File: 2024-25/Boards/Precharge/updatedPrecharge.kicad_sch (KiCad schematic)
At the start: 22 parts, among them J2 43045-0812, Q1 DMN2056U, Q2 DMP2035U, Q3 DMP2035U, Q4 DMP2035U, U1 LM358DR2G

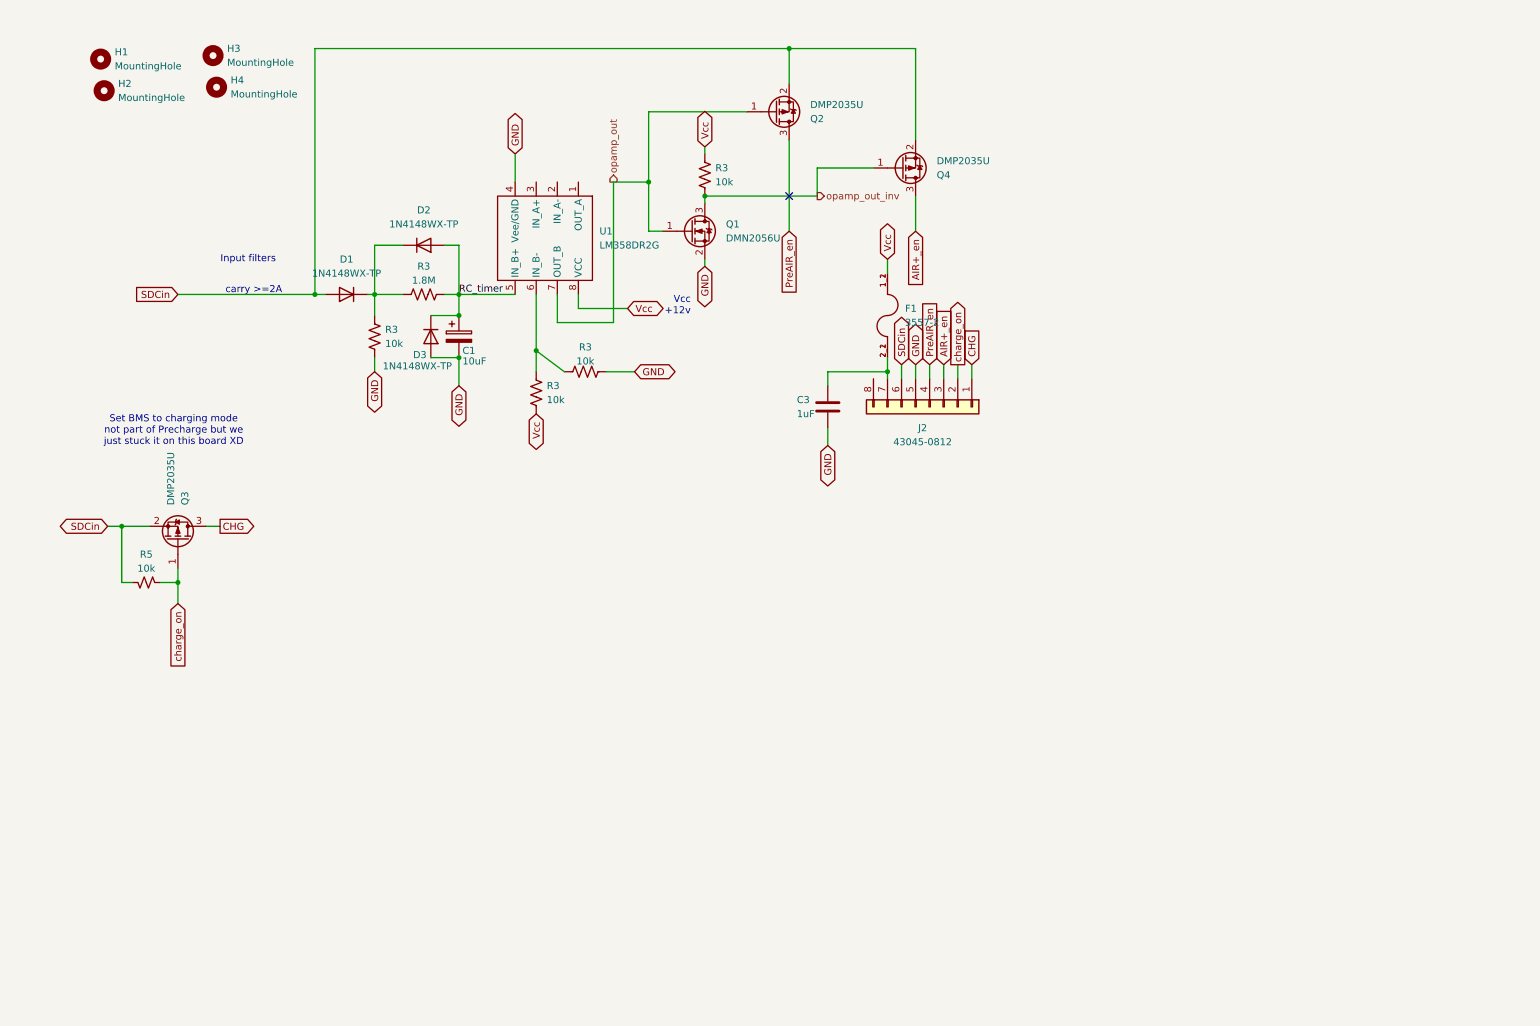
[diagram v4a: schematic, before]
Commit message: new Precharge circuit schm
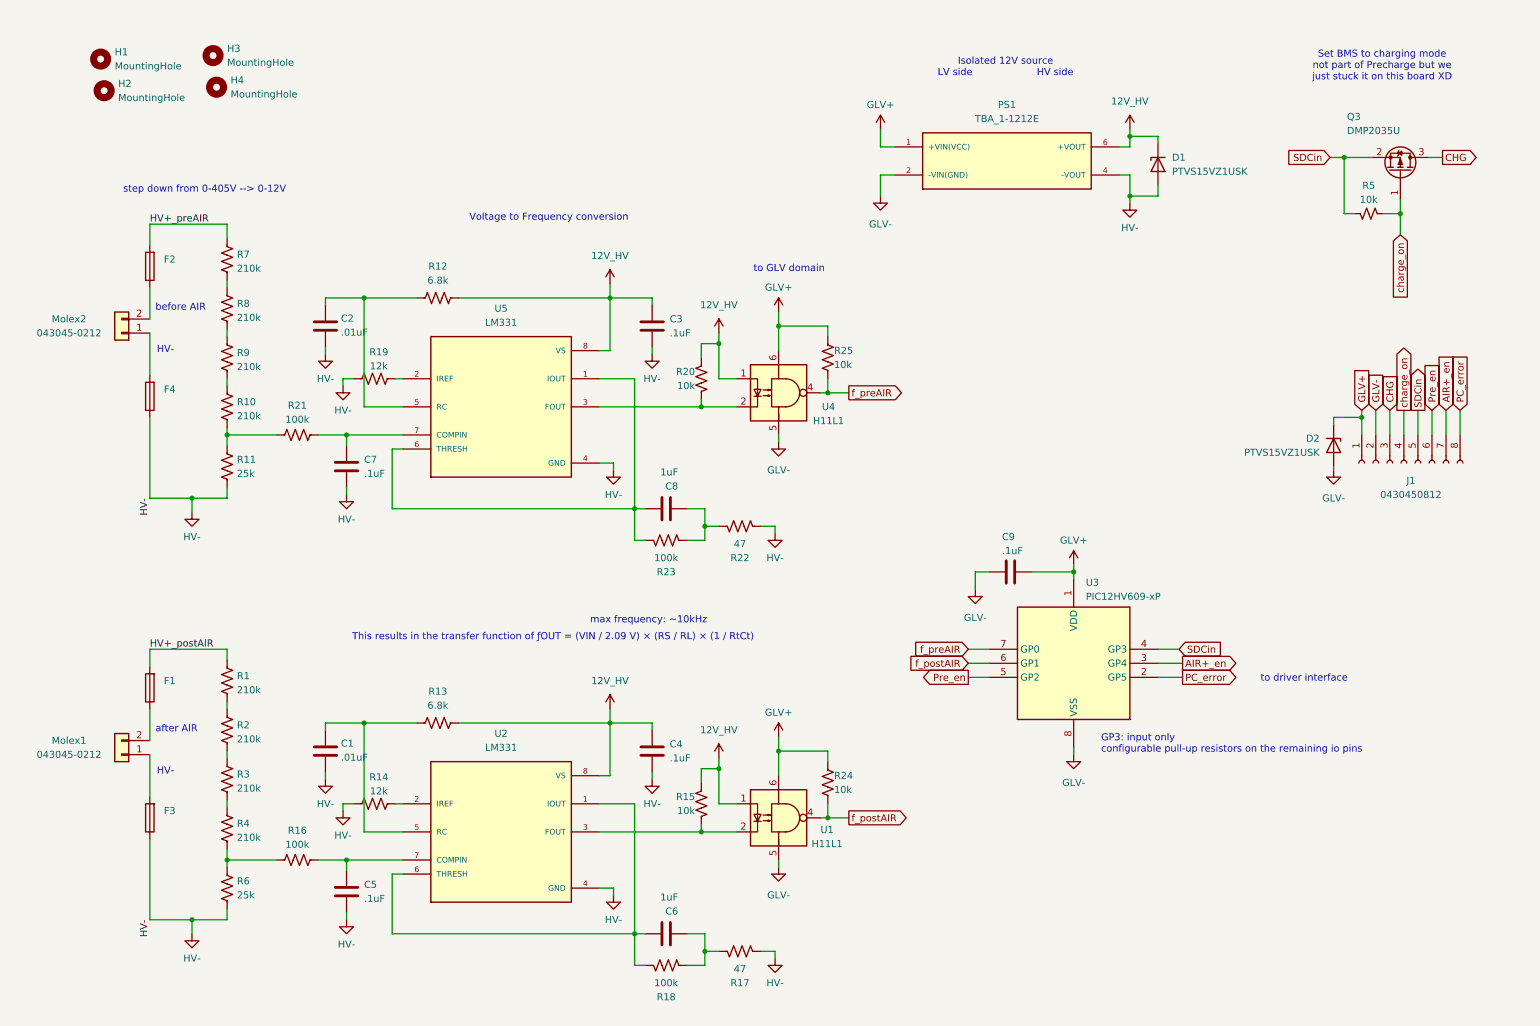
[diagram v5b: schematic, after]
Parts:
- removed C1: 10uF, Capacitor_SMD:C_1206_3216Metric_Pad1.33x1.80mm_HandSolder, symbol Device:C_Polarized
- removed D1, D2, D3: 1N4148WX-TP, Diode_SMD:D_SOD-323, symbol Diode:BAV302
- removed F1: 3557-2, Fuseholder:fuse, symbol 3557-2:3557-2
- removed J2: 43045-0812, Connector_Molex:Molex_Micro-Fit_3.0_43045-0812_2x04_P3.00mm_Vertical, symbol Connector_Generic:Conn_01x08
- removed Q1: DMN2056U, Package_TO_SOT_SMD:SOT-23, symbol Transistor_FET:DMN2056U
- removed Q2, Q4: DMP2035U, Package_TO_SOT_SMD:SOT-23, symbol Transistor_FET:AO3401A
- removed R3 (x4): 10k, Resistor_SMD:R_0805_2012Metric_Pad1.20x1.40mm_HandSolder, symbol Device:R_US
- removed R3: 1.8M, Resistor_SMD:R_0805_2012Metric_Pad1.20x1.40mm_HandSolder, symbol Device:R_US
- removed U1: LM358DR2G, Package_SO:SOIC-8_3.9x4.9mm_P1.27mm, symbol Amplifier_Operational:LM358_whole_unit
- added C1, C2: .01uF, Capacitor_SMD:C_0603_1608Metric, symbol Device:C
- added C4, C5, C7, C9: .1uF, Capacitor_SMD:C_0603_1608Metric, symbol Device:C
- added C6, C8: 1uF, Capacitor_SMD:C_0603_1608Metric, symbol Device:C
- added D1, D2: PTVS15VZ1USK, Diode_SMD:Nexperia_DSN1608-2_1.6x0.8mm, symbol Diode:PTVS15VZ1USK
- added F1, F2, F3, F4: 750mA, Library:FUSE_BK_PCS, symbol Device:Fuse
- added J1: 0430450812, Connector_Molex:Molex_Micro-Fit_3.0_43045-0812_2x04_P3.00mm_Vertical, symbol Connector:Conn_01x08_Socket
- added Molex1, Molex2: 043045-0212, Connector_Molex:Molex_Micro-Fit_3.0_43045-0212_2x01_P3.00mm_Vertical, symbol Connector_Generic:Conn_01x02
- added PS1: TBA_1-1212E, TBA_1-1212E:CONV_TBA_1-1212E, symbol TBA_1-1212E:TBA_1-1212E
- added R1, R10, R2, R3, R4, R7, R8, R9: 210k, Resistor_SMD:R_1206_3216Metric, symbol Device:R_US
- added R11, R6: 25k, Resistor_SMD:R_0603_1608Metric, symbol Device:R_US
- added R12, R13: 6.8k, Resistor_SMD:R_0603_1608Metric, symbol Device:R_US
- added R14, R19: 12k, Resistor_SMD:R_0603_1608Metric, symbol Device:R_US
- added R15, R20, R24, R25: 10k, Resistor_SMD:R_0603_1608Metric, symbol Device:R_US
- added R16, R18, R21, R23: 100k, Resistor_SMD:R_0603_1608Metric, symbol Device:R_US
- added R17, R22: 47, Resistor_SMD:R_0603_1608Metric, symbol Device:R_US
- added U1, U4: H11L1, symbol Isolator:H11L1
- added U2, U5: LM331, LM331:DIP794W45P254L959H508Q8, symbol LM331:LM331
- added U3: PIC12HV609-xP, Package_DIP:DIP-8_W7.62mm, symbol MCU_Microchip_PIC12:PIC12HV609-xP
- C3: value 1uF -> .1uF; footprint Capacitor_SMD:C_0805_2012Metric_Pad1.18x1.45mm_HandSolder -> Capacitor_SMD:C_0603_1608Metric
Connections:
- net AIR+_en: now also J1.7 (Pin_7), U3.3 (GP4)
- net CHG: now also J1.3 (Pin_3)
- net SDCin: now also J1.5 (Pin_5), U3.4 (GP3)
- net charge_on: now also J1.4 (Pin_4)
- net 12V_HV: now reaches C3.1
- net 12V_HV: now also C4.1, D1.1 (K), PS1.6 (+VOUT), R12.2, R13.2, R15.1, R20.1, U1.1, U2.8 (VS), U4.1, U5.8 (VS)
- net GND renamed HV-
- net HV-: now also C1.2, C2.2, C4.2, C5.2, C7.2, D1.2 (A), F3.1, F4.1, PS1.4 (-VOUT), R11.2, R14.1, R17.2, R19.1, R22.2, R6.2, U2.4 (GND), U5.4 (GND)
- new net: C2.1, R12.1, U5.5 (RC)
- new net: R1.2, R2.1
- new net: R16.1, R4.2, R6.1
- new net: C5.1, R16.2, U2.7 (COMPIN)
- new net: C1.1, R13.1, U2.5 (RC)
- new net: R7.2, R8.1
- new net: R8.2, R9.1
- new net: F4.2, Molex2.1 (Pin_1)
- new net: F2.1, Molex2.2 (Pin_2)
- new net: R19.2, U5.2 (IREF)
- new net: C6.1, R18.1, U2.1 (IOUT), U2.6 (THRESH)
- new net: R14.2, U2.2 (IREF)
- new net: R15.2, U1.2, U2.3 (FOUT)
- new net: R20.2, U4.2, U5.3 (FOUT)
- new net: C6.2, R17.1, R18.2
- new net: C8.1, R23.1, U5.1 (IOUT), U5.6 (THRESH)
- new net: C7.1, R21.2, U5.7 (COMPIN)
- new net: C8.2, R22.1, R23.2
- new net: R3.2, R4.1
- new net: R10.1, R9.2
- new net: R10.2, R11.1, R21.1
- new net: R2.2, R3.1
- new net: F3.2, Molex1.1 (Pin_1)
- new net: F1.1, Molex1.2 (Pin_2)
- new net GLV+: C9.1, D2.1 (K), J1.1 (Pin_1), PS1.1 (+VIN(VCC)), R24.1, R25.1, U1.6, U3.1 (VDD), U4.6
- new net GLV-: C9.2, D2.2 (A), J1.2 (Pin_2), PS1.2 (-VIN(GND)), U1.5, U3.8 (VSS), U4.5
- new net HV+_postAIR: F1.2, R1.1
- new net HV+_preAIR: F2.2, R7.1
- new net PC_error: J1.8 (Pin_8), U3.2 (GP5)
- new net Pre_en: J1.6 (Pin_6), U3.5 (GP2)
- new net f_postAIR: R24.2, U1.4, U3.6 (GP1)
- new net f_preAIR: R25.2, U3.7 (GP0), U4.4
- no-connect marks 1 -> 0
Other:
- note added: "GP3: input only configurable pull-up resistors on the remaining io pins"
- note added: "HV-"
- note added: "Isolated 12V source LV side HV side"
- note added: "This results in the transfer function of ƒOUT = (VIN / 2.09 V) × (RS / RL) × (1 / RtCt)"
- note added: "Voltage to Frequency conversion"
- note added: "after AIR"
- note added: "before AIR"
- note added: "max frequency: ~10kHz"
- note added: "step down from 0-405V --> 0-12V"
- note added: "to GLV domain"
- note added: "to driver interface"
- note removed: "Input filters"
- note removed: "Vcc +12v"
- note removed: "carry >=2A"
- moved on the sheet: Q3, R5

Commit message: added LDO
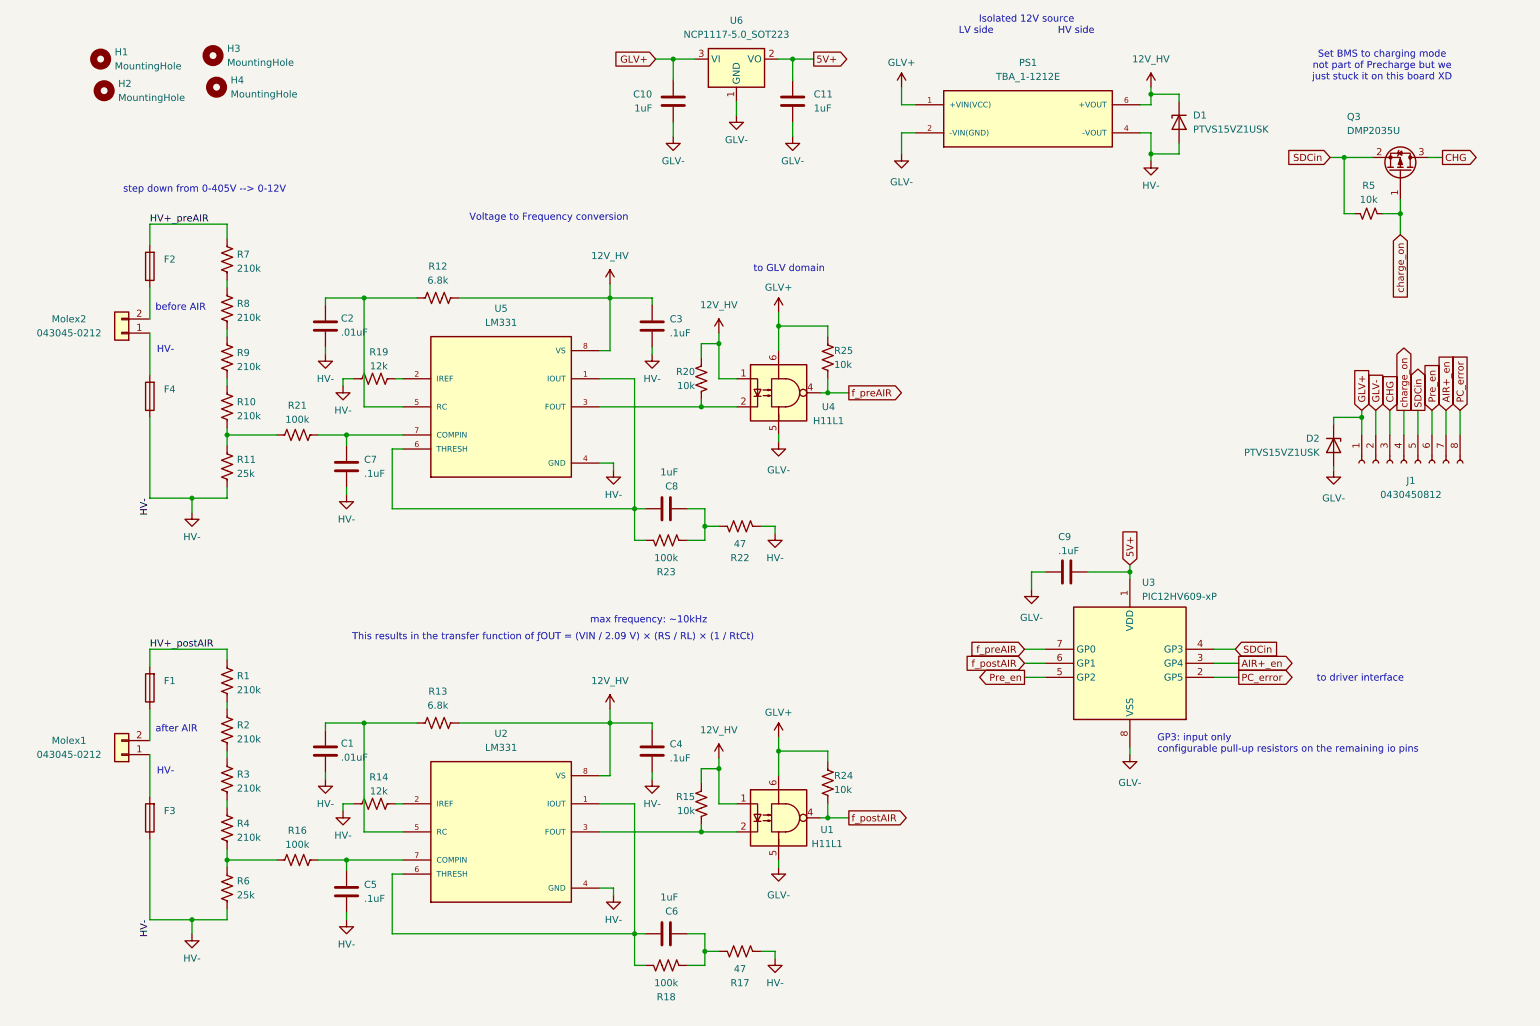
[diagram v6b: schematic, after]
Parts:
- added C10, C11: 1uF, Capacitor_SMD:C_0805_2012Metric_Pad1.18x1.45mm_HandSolder, symbol Device:C
- added U6: NCP1117-5.0_SOT223, Package_TO_SOT_SMD:SOT-223-3_TabPin2, symbol Regulator_Linear:NCP1117-5.0_SOT223
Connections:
- net GLV+: now also C10.1, U6.3 (VI); no longer C9.1, U3.1 (VDD)
- net GLV-: now also C10.2, C11.2, U6.1 (GND)
- new net 5V+: C11.1, C9.1, U3.1 (VDD), U6.2 (VO)
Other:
- moved on the sheet: C9, D1, PS1, U3

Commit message: fixed enable signal
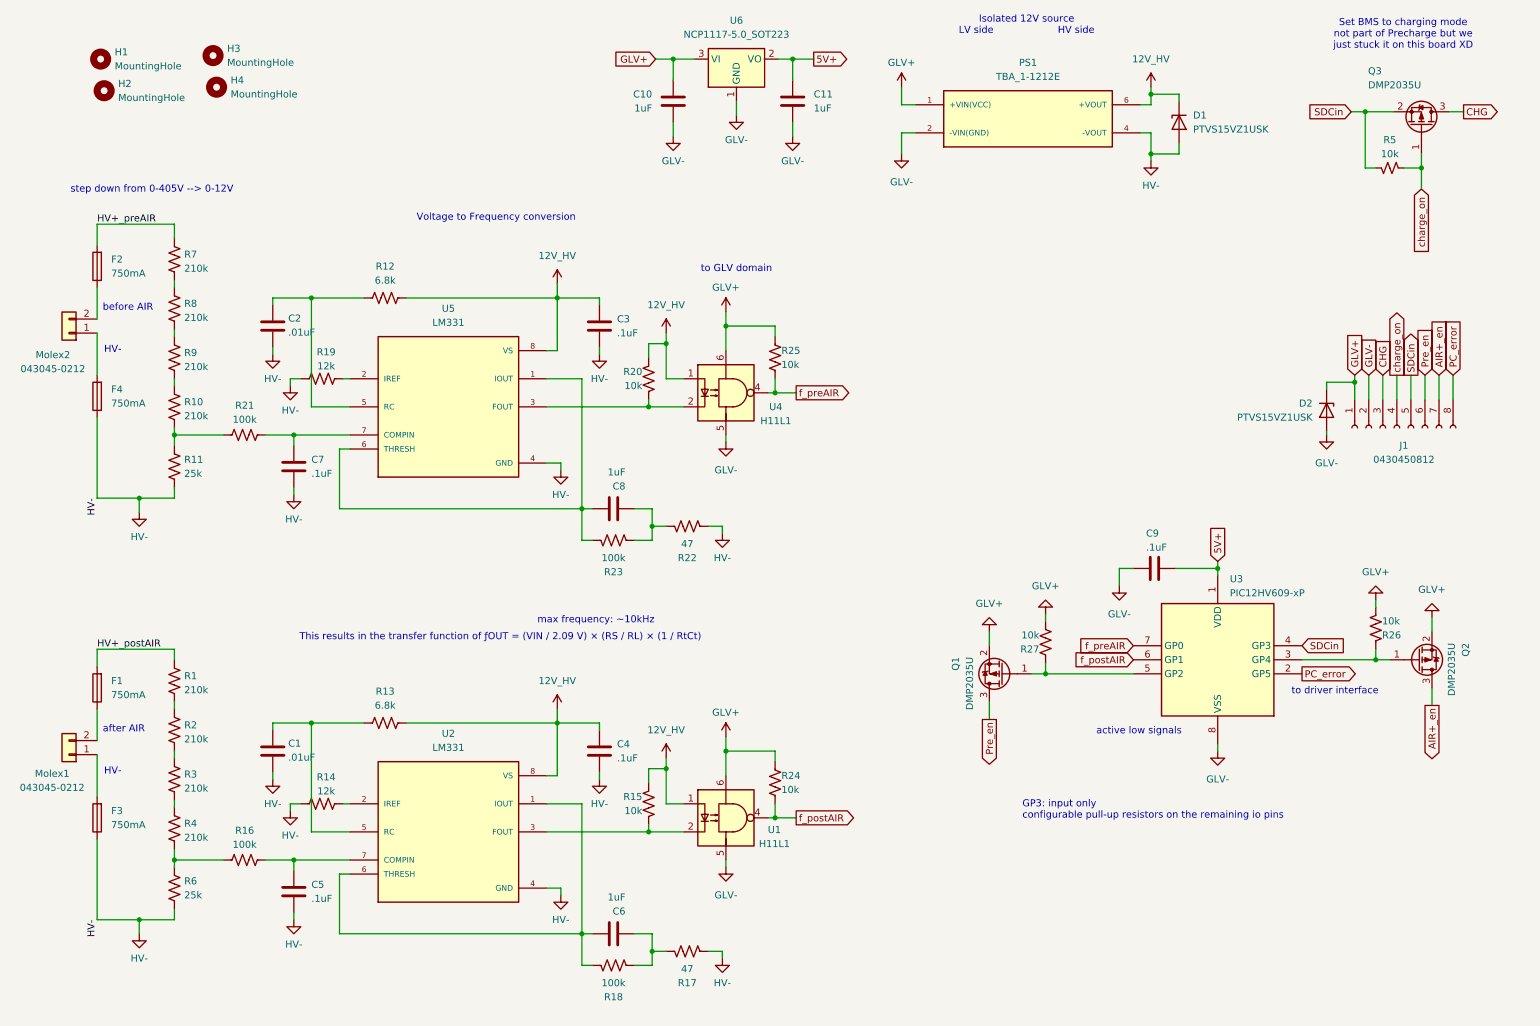
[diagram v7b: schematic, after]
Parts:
- added Q1, Q2: DMP2035U, Package_TO_SOT_SMD:SOT-23, symbol Transistor_FET:AO3401A
- added R26, R27: 10k, Resistor_SMD:R_0603_1608Metric, symbol Device:R_US
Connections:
- net AIR+_en: now also Q2.3 (D); no longer U3.3 (GP4)
- net GLV+: now also Q1.2 (S), Q2.2 (S), R26.2, R27.2
- net Pre_en: now also Q1.3 (D); no longer U3.5 (GP2)
- new net: Q2.1 (G), R26.1, U3.3 (GP4)
- new net: Q1.1 (G), R27.1, U3.5 (GP2)
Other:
- note added: "active low signals"
- moved on the sheet: C1, C2, C3, C4, C5, C6, C7, C8, C9, D2, F2, F4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

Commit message: fixed relay signal
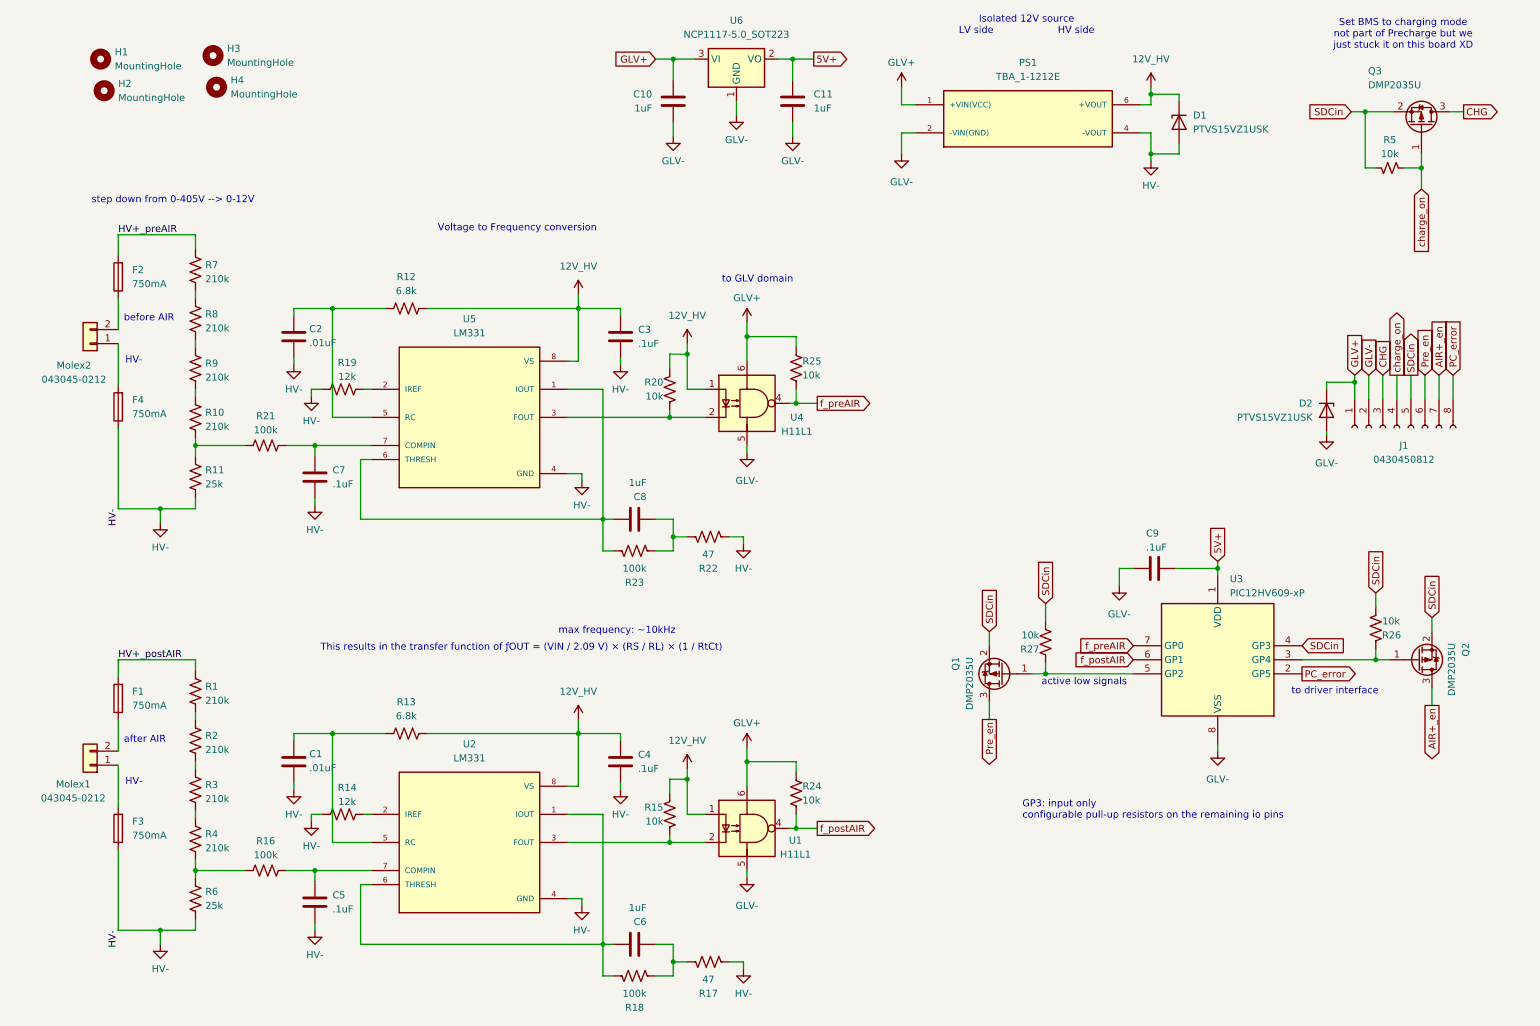
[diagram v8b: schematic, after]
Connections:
- net GLV+: no longer Q1.2 (S), Q2.2 (S), R26.2, R27.2
- net SDCin: now also Q1.2 (S), Q2.2 (S), R26.2, R27.2
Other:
- moved on the sheet: C1, C2, C3, C4, C5, C6, C7, C8, F1, F2, F3, F4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
